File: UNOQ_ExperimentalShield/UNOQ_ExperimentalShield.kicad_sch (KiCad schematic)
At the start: 74 parts, among them CN1 485, CN2 USB, CN3 Can, CN4 Can, CN5 485, J1 Power, J2 Digital/PWM, J3 Analog, J4 Digital/PWM, Q2 SS8050, SW1 Usr1, SW2 Usr1, SW3 Usr1, SW4 Usr1, U1 25LCxxx, U2 LM35-D, U3 MAX3485EESA+T, U4 CH340N, U5 TJA1051T-3

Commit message: minor
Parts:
- removed JP5, JP6: RS485 Term, Connector_PinHeader_2.54mm:PinHeader_1x02_P2.54mm_Vertical, symbol Jumper:Jumper_2_Open
- removed R15, R16, R17, R79: 1k, Resistor_SMD:R_0402_1005Metric, symbol Device:R
- added JP5: Jmp, Connector_PinHeader_2.54mm:PinHeader_2x02_P2.54mm_Vertical, symbol Connector_Generic:Conn_02x02_Odd_Even
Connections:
- net +3V3: now also RV1.1, RV2.1
- net CANL: now also JP5.3 (Pin_3)
- net GND: now also RV1.3, RV2.3
- net 485_T_A: now reaches R23.2
- net 485_T_A: now also JP5.2 (Pin_2)
- net CAN_T_H: now reaches R27.2
- net CAN_T_H: now also JP5.4 (Pin_4)
- net B renamed 485_T_B
- net 485_T_B: now also JP5.1 (Pin_1)

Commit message: minor
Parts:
- added C5: 100nF, Capacitor_SMD:C_0402_1005Metric, symbol Device:C
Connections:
- net +3V3: now also C5.1; no longer C4.1
- net +5V: now also C4.1
- net GND: now also C5.2
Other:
- moved on the sheet: C3
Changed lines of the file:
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@@
 	(wire
 		(pts
+			(xy 189.23 179.07) (xy 189.23 181.61)
+		)
+		(stroke
+			(width 0)
+			(type default)
+		)
+	)
+	(wire
+		(pts
 			(xy 166.37 57.15) (xy 163.83 57.15)
 		)
@@
 	(wire
 		(pts
+			(xy 189.23 168.91) (xy 189.23 171.45)
+		)
+		(stroke
+			(width 0)
+			(type default)
+		)
+	)
+	(wire
+		(pts
 			(xy 166.37 54.61) (xy 163.83 54.61)
 		)
@@
 	(wire
 		(pts
+			(xy 250.19 48.26) (xy 250.19 50.8)
+		)
+		(stroke
+			(width 0)
+			(type default)
+		)
+	)
+	(wire
+		(pts
 			(xy 95.25 120.65) (xy 95.25 123.19)
 		)
@@
 	(wire
 		(pts
-			(xy 189.23 158.75) (xy 189.23 161.29)
-		)
-		(stroke
-			(width 0)
-			(type default)
-		)
-	)
-	(wire
-		(pts
 			(xy 39.37 72.39) (xy 26.67 72.39)
 		)
@@
 	(wire
 		(pts
+			(xy 250.19 58.42) (xy 250.19 60.96)
+		)
+		(stroke
+			(width 0)
+			(type default)
+		)
+	)
+	(wire
+		(pts
 			(xy 204.47 213.36) (xy 204.47 215.9)
 		)
@@
 	(wire
 		(pts
-			(xy 189.23 168.91) (xy 189.23 171.45)
-		)
-		(stroke
-			(width 0)
-			(type default)
-		)
-	)
-	(wire
-		(pts
 			(xy 306.07 34.29) (xy 306.07 36.83)
 		)
@@
 		)
 	)
-	(label "3V3"
-		(at 226.06 232.41 90)
-		(effects
-			(font
-				(size 1.27 1.27)
-			)
-			(justify left bottom)
-		)
-	)
 	(label "B"
 		(at 220.98 64.77 180)
@@
 		)
 	)
+	(label "3V3"
+		(at 250.19 48.26 90)
+		(effects
+			(font
+				(size 1.27 1.27)
+			)
+			(justify left bottom)
+		)
+	)
 	(label "RX_USB"
 		(at 33.02 219.71 180)
@@
 		)
 	)
-	(label "3V3"
-		(at 189.23 158.75 90)
-		(effects
-			(font
-				(size 1.27 1.27)
-			)
-			(justify left bottom)
-		)
-	)
 	(label "CANRX"
 		(at 204.47 161.29 180)
@@
 		)
 	)
+	(label "5V"
+		(at 226.06 232.41 90)
+		(effects
+			(font
+				(size 1.27 1.27)
+			)
+			(justify left bottom)
+		)
+	)
 	(label "D11{slash}MOSI"
 		(at 80.01 49.53 0)
@@
 		)
 	)
+	(label "3V3"
+		(at 189.23 168.91 90)
+		(effects
+			(font
+				(size 1.27 1.27)
+			)
+			(justify left bottom)
+		)
+	)
 	(label "A"
 		(at 256.54 34.29 180)
@@
 	)
 	(symbol
+		(lib_id "Device:C")
+		(at 189.23 175.26 0)
+		(unit 1)
+		(exclude_from_sim no)
+		(in_bom yes)
+		(on_board yes)
+		(dnp no)
+		(fields_autoplaced yes)
+		(property "Reference" "C5"
+			(at 192.405 173.9899 0)
+			(effects
+				(font
+					(size 1.27 1.27)
+				)
+				(justify left)
+			)
+		)
+		(property "Value" "100nF"
+			(at 192.405 176.5299 0)
+			(effects
+				(font
+					(size 1.27 1.27)
+				)
+				(justify left)
+			)
+		)
+		(property "Footprint" "Capacitor_SMD:C_0402_1005Metric"
+			(at 190.1952 179.07 0)
+			(effects
+				(font
+					(size 1.27 1.27)
+				)
+				(hide yes)
+			)
+		)
+		(property "Datasheet" "~"
+			(at 189.23 175.26 0)
+			(effects
+				(font
+					(size 1.27 1.27)
+				)
+				(hide yes)
+			)
+		)
+		(property "Description" ""
+			(at 189.23 175.26 0)
+			(effects
+				(font
+					(size 1.27 1.27)
+				)
+			)
+		)
+		(property "LCSC" "C155422"
+			(at 189.23 175.26 0)
+			(effects
+				(font
+					(size 1.27 1.27)
+				)
+				(hide yes)
+			)
+		)
+		(pin "1"
+		)
+		(pin "2"
+		)
+		(instances
+			(project "UNOQ_ExperimentalShield"
+				(path "/e63e39d7-6ac0-4ffd-8aa3-1841a4541b55"
+					(reference "C5")
+					(unit 1)
+				)
+			)
+		)
+	)
+	(symbol
 		(lib_id "Memory_EEPROM:25LCxxx")
 		(at 181.61 229.87 0)
@@
 	)
 	(symbol
+		(lib_id "power:GND")
+		(at 189.23 181.61 0)
+		(unit 1)
+		(exclude_from_sim no)
+		(in_bom yes)
+		(on_board yes)
+		(dnp no)
+		(property "Reference" "#PWR012"
+			(at 189.23 187.96 0)
+			(effects
+				(font
+					(size 1.27 1.27)
+				)
+				(hide yes)
+			)
+		)
+		(property "Value" "GND"
+			(at 189.23 186.055 0)
+			(effects
+				(font
+					(size 1.27 1.27)
+				)
+			)
+		)
+		(property "Footprint" ""
+			(at 189.23 181.61 0)
+			(effects
+				(font
+					(size 1.27 1.27)
+				)
+				(hide yes)
+			)
+		)
+		(property "Datasheet" ""
+			(at 189.23 181.61 0)
+			(effects
+				(font
+					(size 1.27 1.27)
+				)
+				(hide yes)
+			)
+		)
+		(property "Description" ""
+			(at 189.23 181.61 0)
+			(effects
+				(font
+					(size 1.27 1.27)
+				)
+			)
+		)
+		(pin "1"
+		)
+		(instances
+			(project "UNOQ_ExperimentalShield"
+				(path "/e63e39d7-6ac0-4ffd-8aa3-1841a4541b55"
+					(reference "#PWR012")
+					(unit 1)
+				)
+			)
+		)
+	)
+	(symbol
 		(lib_id "Device:R")
 		(at 250.19 129.54 0)
@@
 	(symbol
 		(lib_id "Device:C")
-		(at 189.23 165.1 0)
+		(at 250.19 54.61 0)
 		(unit 1)
 		(exclude_from_sim no)
@@
 		(fields_autoplaced yes)
 		(property "Reference" "C3"
-			(at 192.405 163.8299 0)
+			(at 253.365 53.3399 0)
 			(effects
 				(font
@@
 		)
 		(property "Value" "100nF"
-			(at 192.405 166.3699 0)
+			(at 253.365 55.8799 0)
 			(effects
 				(font
@@
 		)
 		(property "Footprint" "Capacitor_SMD:C_0402_1005Metric"
-			(at 190.1952 168.91 0)
+			(at 251.1552 58.42 0)
 			(effects
 				(font
@@
 		)
 		(property "Datasheet" "~"
-			(at 189.23 165.1 0)
+			(at 250.19 54.61 0)
 			(effects
 				(font
@@
 		)
 		(property "Description" ""
-			(at 189.23 165.1 0)
+			(at 250.19 54.61 0)
 			(effects
 				(font
@@
 		)
 		(property "LCSC" "C155422"
-			(at 189.23 165.1 0)
+			(at 250.19 54.61 0)
 			(effects
 				(font
@@
 	(symbol
 		(lib_id "power:GND")
-		(at 189.23 171.45 0)
+		(at 250.19 60.96 0)
 		(unit 1)
 		(exclude_from_sim no)
@@
 		(dnp no)
 		(property "Reference" "#PWR029"
-			(at 189.23 177.8 0)
+			(at 250.19 67.31 0)
 			(effects
 				(font
@@
 		)
 		(property "Value" "GND"
-			(at 189.23 175.895 0)
+			(at 250.19 65.405 0)
 			(effects
 				(font
@@
 		)
 		(property "Footprint" ""
-			(at 189.23 171.45 0)
+			(at 250.19 60.96 0)
 			(effects
 				(font
@@
 		)
 		(property "Datasheet" ""
-			(at 189.23 171.45 0)
+			(at 250.19 60.96 0)
 			(effects
 				(font
@@
 		)
 		(property "Description" ""
-			(at 189.23 171.45 0)
+			(at 250.19 60.96 0)
 			(effects
 				(font

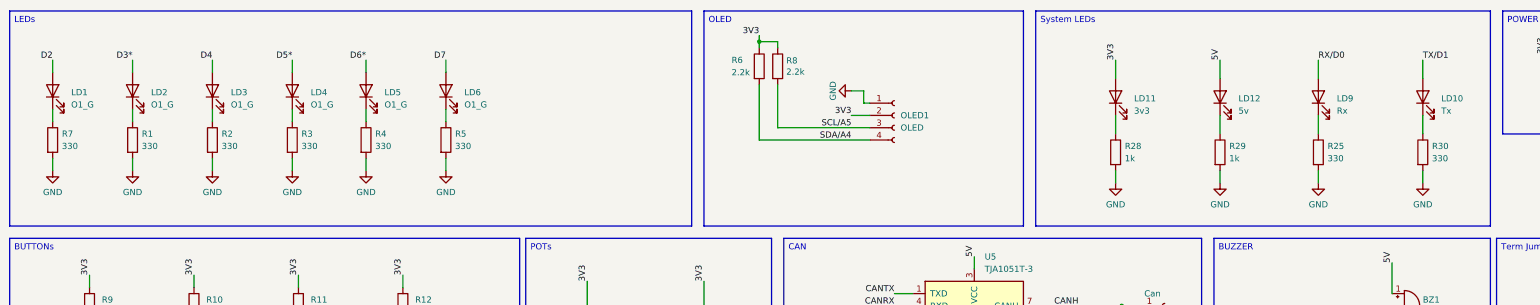
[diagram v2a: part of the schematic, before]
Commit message: Some fixes: - Fixed labesl dimension - Fixed resistor values for leds - Fixed OLED footprint - Added HW version
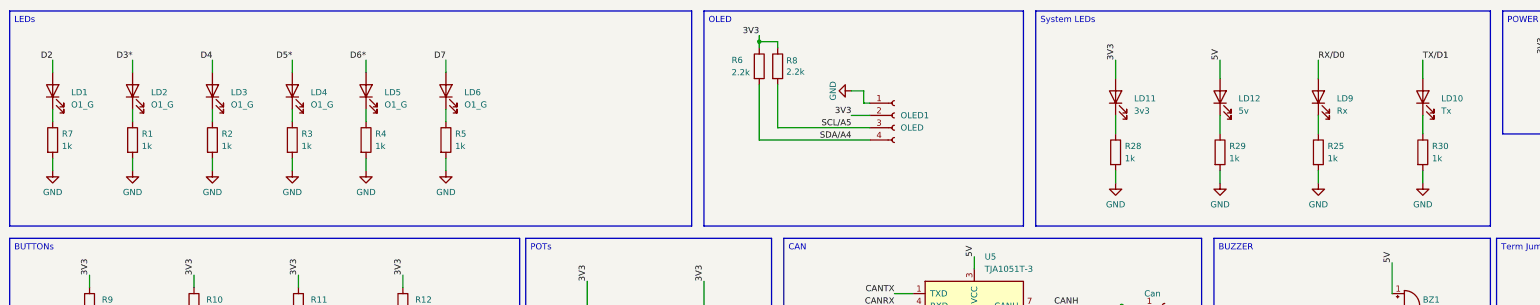
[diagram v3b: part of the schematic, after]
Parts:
- OLED1: footprint oled:MODULE_DM-OLED096-636 -> oled:OLED096
- R1, R2, R25, R3, R30, R4, R5, R7: value 330 -> 1k; LCSC C25104 -> C140196
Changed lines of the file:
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@@
 			)
 		)
-		(property "Value" "330"
+		(property "Value" "1k"
 			(at 48.895 128.2699 0)
 			(effects
@@
 			)
 		)
-		(property "LCSC" "C25104"
+		(property "LCSC" "C140196"
 			(at 46.99 127 0)
 			(effects
@@
 			)
 		)
-		(property "Value" "330"
+		(property "Value" "1k"
 			(at 97.155 128.2699 0)
 			(effects
@@
 			)
 		)
-		(property "LCSC" "C25104"
+		(property "LCSC" "C140196"
 			(at 95.25 127 0)
 			(effects
@@
 			)
 		)
-		(property "Value" "330"
+		(property "Value" "1k"
 			(at 81.915 128.2699 0)
 			(effects
@@
 			)
 		)
-		(property "LCSC" "C25104"
+		(property "LCSC" "C140196"
 			(at 80.01 127 0)
 			(effects
@@
 			)
 		)
-		(property "Value" "330"
+		(property "Value" "1k"
 			(at 315.595 130.8099 0)
 			(effects
@@
 			)
 		)
-		(property "LCSC" "C25104"
+		(property "LCSC" "C140196"
 			(at 313.69 129.54 0)
 			(effects
@@
 			)
 		)
-		(property "Footprint" "oled:MODULE_DM-OLED096-636"
+		(property "Footprint" "oled:OLED096"
 			(at 204.47 121.92 0)
 			(effects
@@
 			)
 		)
-		(property "Value" "330"
+		(property "Value" "1k"
 			(at 65.405 128.2699 0)
 			(effects
@@
 			)
 		)
-		(property "LCSC" "C25104"
+		(property "LCSC" "C140196"
 			(at 63.5 127 0)
 			(effects
@@
 			)
 		)
-		(property "Value" "330"
+		(property "Value" "1k"
 			(at 32.385 128.2699 0)
 			(effects
@@
 			)
 		)
-		(property "LCSC" "C25104"
+		(property "LCSC" "C140196"
 			(at 30.48 127 0)
 			(effects
@@
 			)
 		)
-		(property "Value" "330"
+		(property "Value" "1k"
 			(at 113.665 128.2699 0)
 			(effects
@@
 			)
 		)
-		(property "LCSC" "C25104"
+		(property "LCSC" "C140196"
 			(at 111.76 127 0)
 			(effects
@@
 			)
 		)
-		(property "Value" "330"
+		(property "Value" "1k"
 			(at 294.005 130.8099 0)
 			(effects
@@
 			)
 		)
-		(property "LCSC" "C25104"
+		(property "LCSC" "C140196"
 			(at 292.1 129.54 0)
 			(effects

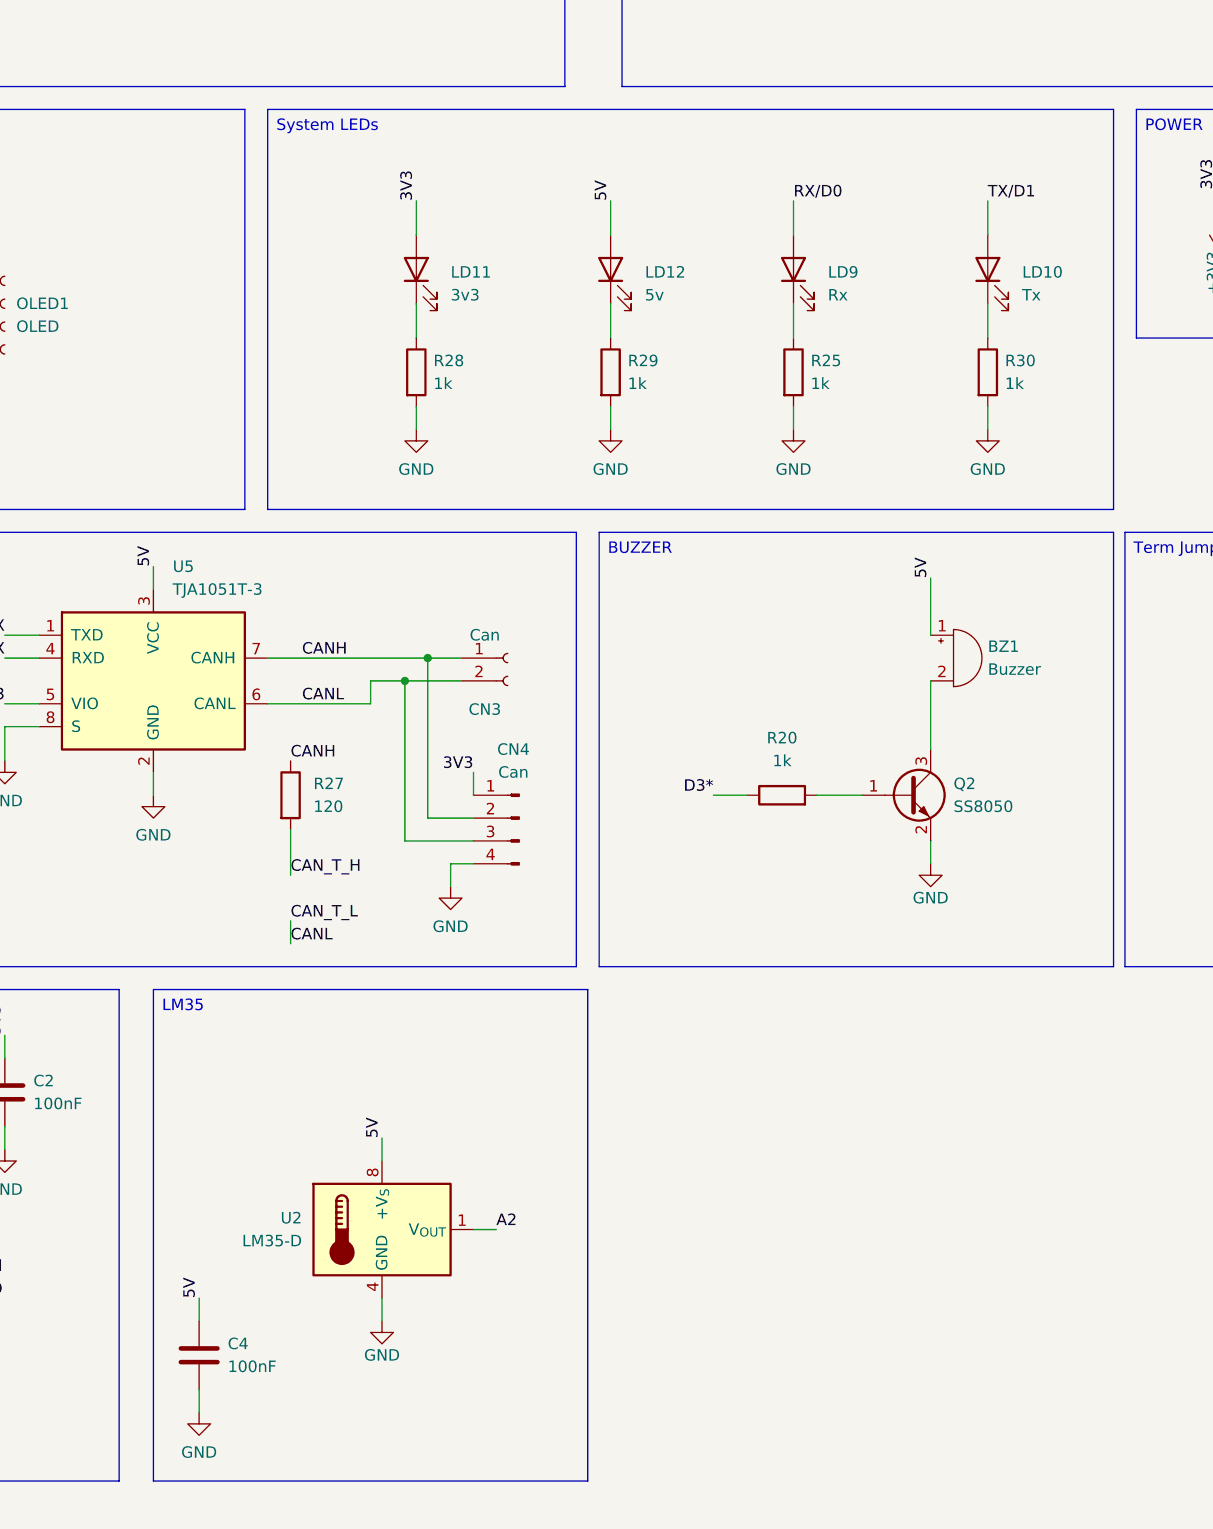
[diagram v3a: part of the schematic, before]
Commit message: Some modifications: - TX/RX Led polarity inverted - LM35 has been replaced with TMP102 (I2C Thermo, better and cheaper) - OLED Shape has been fixed - LED Resistors updated to 1k
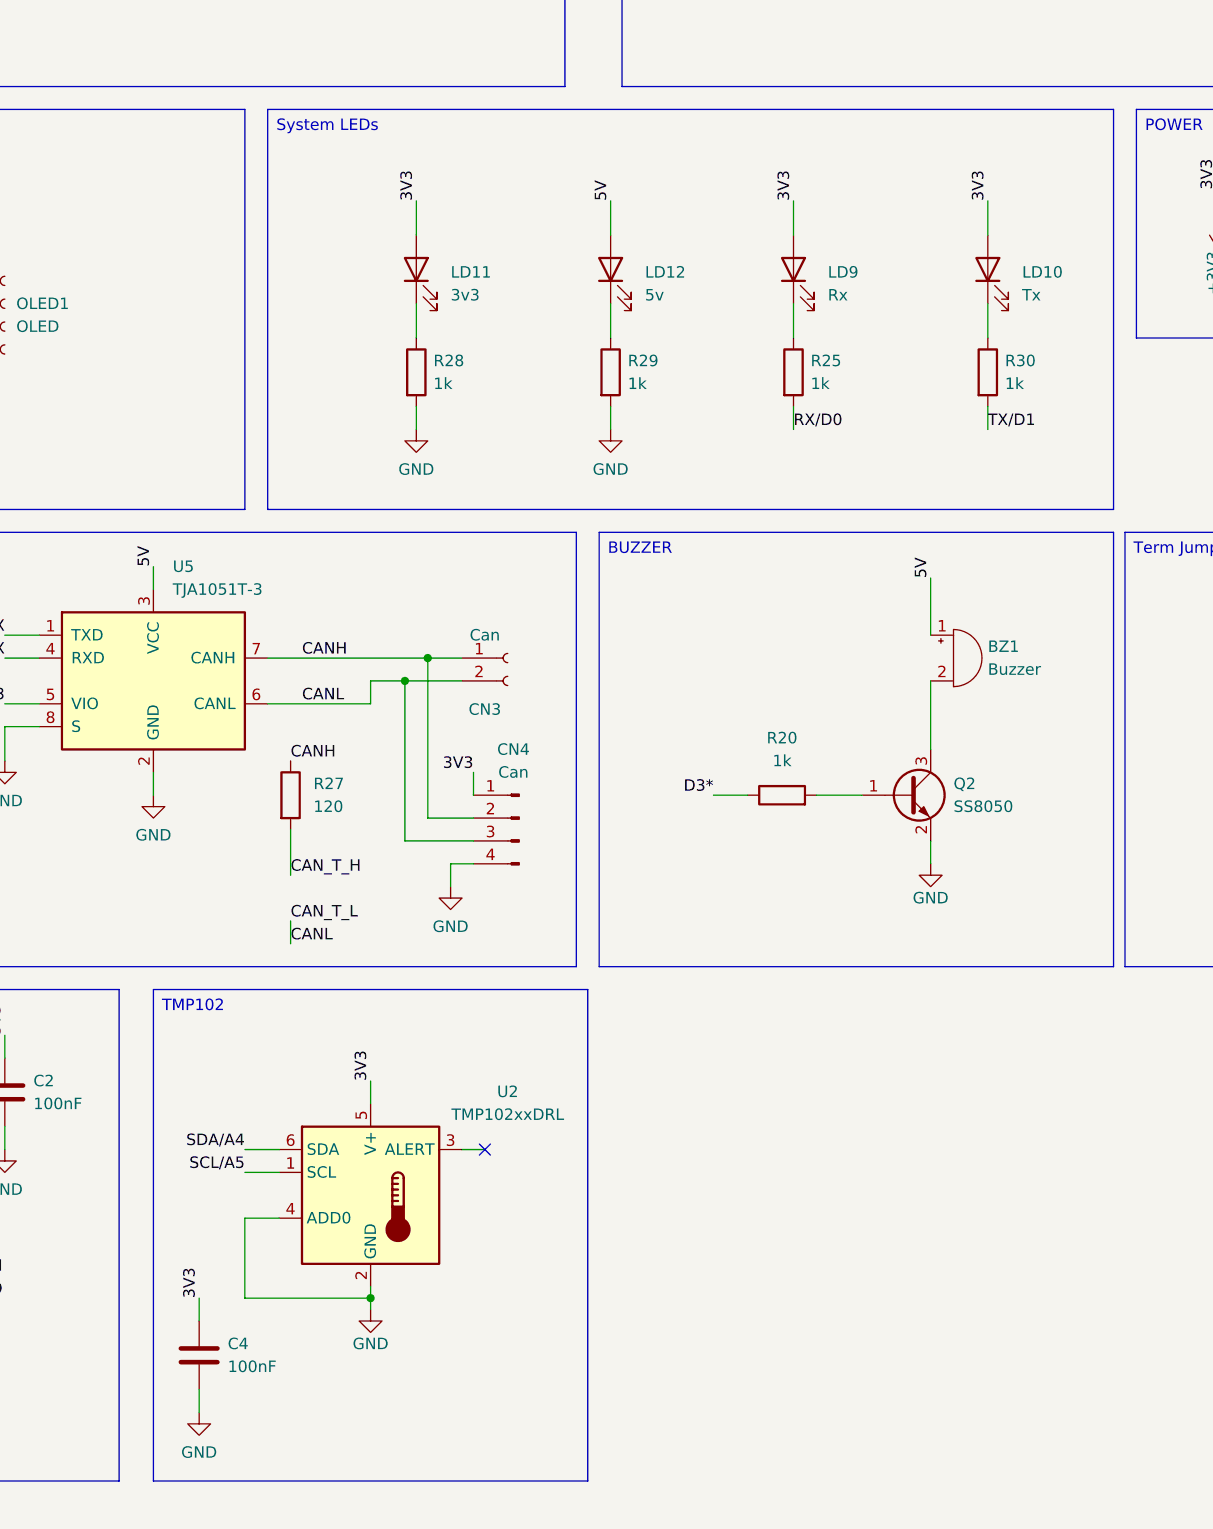
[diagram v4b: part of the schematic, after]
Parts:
- removed U2: LM35-D, Package_SO:SOIC-8_3.9x4.9mm_P1.27mm, symbol Sensor_Temperature:LM35-D
- added U2: TMP102xxDRL, Package_TO_SOT_SMD:SOT-563, symbol Sensor_Temperature:TMP102xxDRL
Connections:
- net +3V3: now also C4.1, LD10.2 (A), LD9.2 (A), U2.5 (V+)
- net +5V: no longer C4.1
- net GND: now also U2.2 (GND), U2.4 (ADD0); no longer R25.2, R30.2
- net RX/D0: now also R25.2; no longer LD9.2 (A)
- net SCL/A5: now also U2.1 (SCL)
- net SDA/A4: now also U2.6 (SDA)
- net TX/D1: now also R30.2; no longer LD10.2 (A)
- no-connect marks 4 -> 5

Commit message: final vesion
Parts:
- removed BZ1: Buzzer, Buzzer_Beeper:Buzzer_12x9.5RM7.6, symbol Device:Buzzer
- removed Q2: SS8050, Package_TO_SOT_SMD:SOT-23, symbol Transistor_BJT:SS8050
- removed R20: 1k, Resistor_SMD:R_0402_1005Metric, symbol Device:R
- added JP6, JP7, JP8: Jmp, Connector_PinHeader_2.54mm:PinHeader_1x03_P2.54mm_Vertical, symbol Jumper:Jumper_3_Open
- added LD7: Rx, LED_SMD:LED_0603_1608Metric, symbol Device:LED
- added LD8: Tx, LED_SMD:LED_0603_1608Metric, symbol Device:LED
- added R15, R16: 1k, Resistor_SMD:R_0402_1005Metric, symbol Device:R
- CN3, CN5: footprint Connector_Phoenix_MC:PhoenixContact_MC_1,5_2-G-3.5_1x02_P3.50mm_Horizontal -> TerminalBlock_Phoenix:TerminalBlock_Phoenix_MPT-0,5-2-2.54_1x02_P2.54mm_Horizontal; LCSC C395830 -> C474920
- U3: value MAX3485EESA+T -> MAX3485ESA-MS; LCSC C9943 -> C7434431
- U5: LCSC (none) -> C38695
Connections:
- net +3V3: now also JP8.1 (A), LD7.2 (A), LD8.2 (A); no longer C1.1, C2.1, C3.1, C5.1, CN4.1 (Pin_1), U1.8 (VCC), U3.8 (VCC), U4.5 (VCC), U5.5 (VIO)
- net +5V: now also C5.1, JP8.3 (B)
- net CANRX: now also JP6.2 (C), R15.2; no longer JP2.1 (A)
- net CANTX: now also JP7.2 (C), R16.2; no longer JP1.1 (A)
- net D6*: now also LD3.2 (A), R11.2, SW3.2; no longer LD5.2 (A)
- net D7: now also LD4.2 (A), R12.2, SW4.2; no longer LD6.2 (A)
- net D8: now also LD5.2 (A)
- net D9*: now also LD6.2 (A)
- removed net D4: J4.4 (Pin_4), LD3.2 (A), R11.2, SW3.2
- removed net D5*: J4.3 (Pin_3), LD4.2 (A), R12.2, SW4.2
- new net: LD7.1 (K), R15.1
- new net: LD8.1 (K), R16.1
- new net CANRX_R4: JP2.1 (A), JP6.1 (A)
- new net CANTX_R4: JP1.1 (A), JP7.1 (A)
- new net D4/FDCAN_TX: J4.4 (Pin_4), JP7.3 (B)
- new net D5*/FDCAN_RX: J4.3 (Pin_3), JP6.3 (B)
- new net Vio: C1.1, C2.1, C3.1, CN4.1 (Pin_1), JP8.2 (C), U1.8 (VCC), U3.8 (VCC), U4.5 (VCC), U5.5 (VIO)
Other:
- moved on the sheet: JP5, LD10, LD11, LD12, LD9, OLED1, R25, R28, R29, R30, R6, R8
